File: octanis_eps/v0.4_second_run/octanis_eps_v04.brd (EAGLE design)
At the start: 61.9 x 49.5 mm, 101 parts, among them IC1 OPA2333DGK, IC5 OPA2333DGK, IC7 OPA2333DGK, IC9 OPA2333DGK, Q1 FC-12M, Q2 N-HEXFET-2D_SOT232-, Q3 N-HEXFET-2D_SOT232-, Q4 N-HEXFET-2D_SOT232-

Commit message: various corrections on EPS v0.3, new v0.4 for second run
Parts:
- removed A_EXT: (no value), jumper:JP4
- removed R37: 50m, rcl:R1206
- added BT_CHG, DSP_CMD: (no value), pinhead:1X01
- added JP2: (no value), jumper:JP4Q
- added U$9: 50m, Octanis1_EPS:4PADS_RESISTOR
- moved R3 0.74 mm to (50.1, 51.4)
- moved R25 0.64 mm to (46.4, 33.6)
- moved R12 0.31 mm to (26.1, 31.8)
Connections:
- new net N$38: R38.1, U$9.I2
- new net N$40: R39.1, U$9.I1
- net A_EXT1: now also JP2.7; no longer A_EXT.4
- net A_EXT2: now also JP2.5; no longer A_EXT.3
- net A_EXT3: now also JP2.3; no longer A_EXT.2
- net A_EXT4: now also JP2.1; no longer A_EXT.1
- net BT+: now also U$9.V1; no longer R37.1, R39.1
- net BT_CHG: now also BT_CHG.1, U$9.V2; no longer R37.2, R38.1
- net GND: now also JP2.2, JP2.4, JP2.6, JP2.8
- net N$45: now also DSP_CMD.1
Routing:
- net BT+: track 129.7 -> 121.5 mm
- net N$40: track 0.00 -> 6.17 mm
- net N$45: track 15.8 -> 17.9 mm
- net N$38: track 0.00 -> 1.85 mm
- net A_EXT4: track 12.8 -> 11.2 mm
- net A_EXT3: track 11.2 -> 9.67 mm
- net EN_HEAT1: track 31.4 -> 32.8 mm
- net BT_CHG: track 2.16 -> 3.38 mm
- net N$12: track 88.9 -> 89.9 mm
- net A_EXT1: track 10.3 -> 9.39 mm
- net A_EXT2: track 11.0 -> 10.2 mm
- net N$23: track 35.2 -> 35.9 mm
- net EN_HEAT3: track 17.4 -> 16.7 mm
- net N$37: track 29.0 -> 29.7 mm
- net SC+: track 12.0 -> 11.3 mm
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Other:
- board text added: "GND1"
- board text added: "GND2"
- board text added: "GND3"
- board text added: "GND4"
- board text added: "Octanis_EPS v0.4"
- board text removed: "Octanis_EPS v0.3"

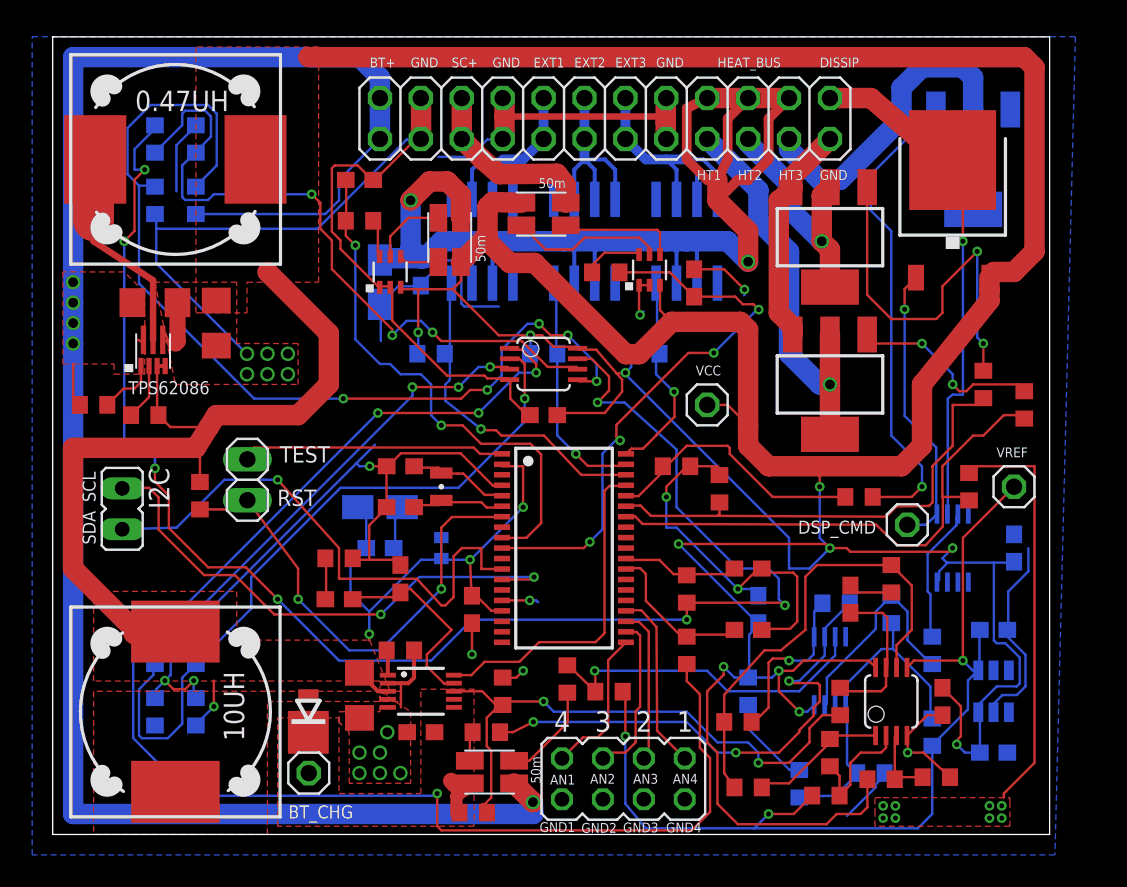
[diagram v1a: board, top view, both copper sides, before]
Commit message: thicker analog tracks for CHGCMD, better analog Grounding (same ref), regenerated gerbers. Checked with Beat
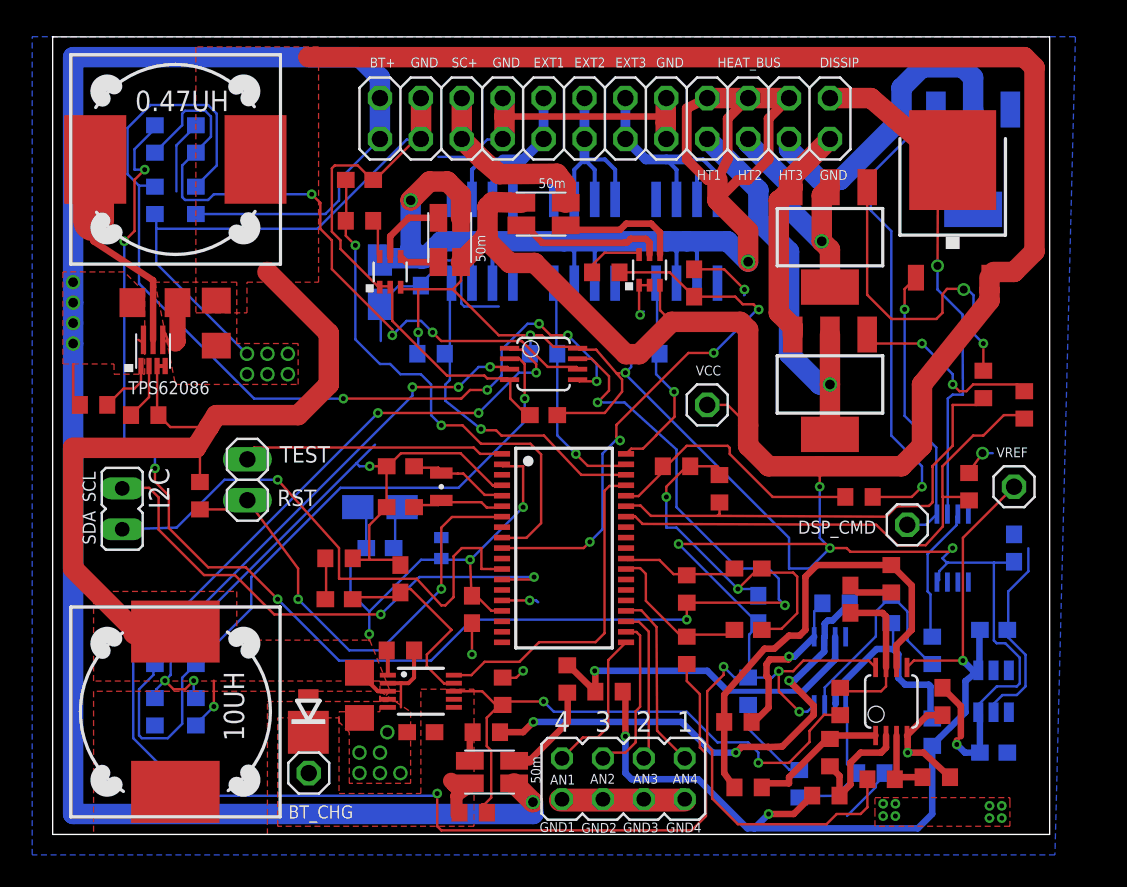
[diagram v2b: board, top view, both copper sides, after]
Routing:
- net GND: track 252.0 -> 235.9 mm, vias 29 -> 30
- net N$31: track 24.4 -> 20.5 mm
- net DISSIP: track 31.9 -> 35.3 mm
- net VREF: track 61.2 -> 60.0 mm
- net N$17: track 32.3 -> 31.2 mm
- net N$20: track 12.4 -> 13.4 mm

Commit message: modified silk screen for EPS
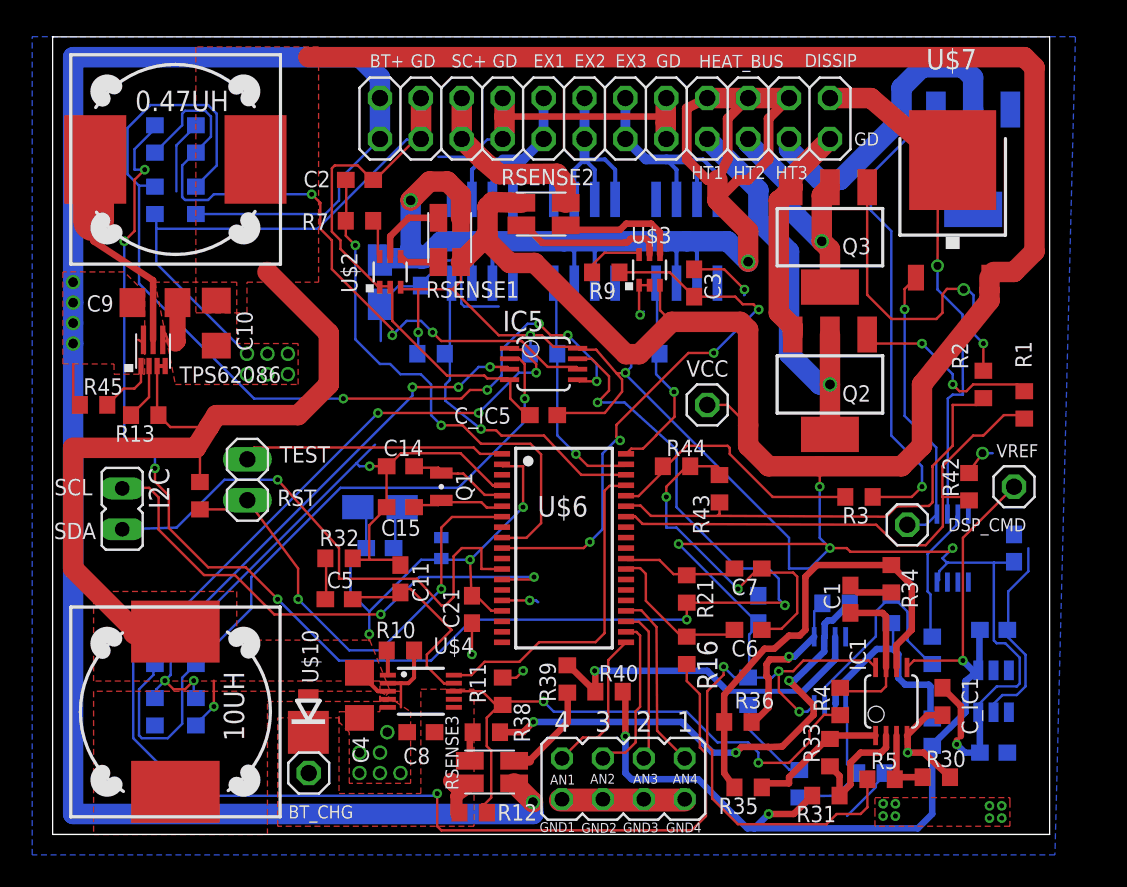
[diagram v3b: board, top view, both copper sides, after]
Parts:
- RSENSE2: value 50m -> RSENSE2
- RSENSE3: value 50m -> RSENSE3
- R_SENSE1: value 50m -> RSENSE1
- renumbered FERRITE_BEAD to FERRITE, U$1 to R_SENSE1, U$8 to RSENSE2, U$9 to RSENSE3
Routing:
- net GND: track 235.9 -> 234.6 mm
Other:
- board text added: "EX1"
- board text added: "EX2"
- board text added: "EX3"
- board text added: "GD"
- board text added: "TPS2022D"
- board text removed: "EXT1"
- board text removed: "EXT2"
- board text removed: "EXT3"
- board text removed: "GND"

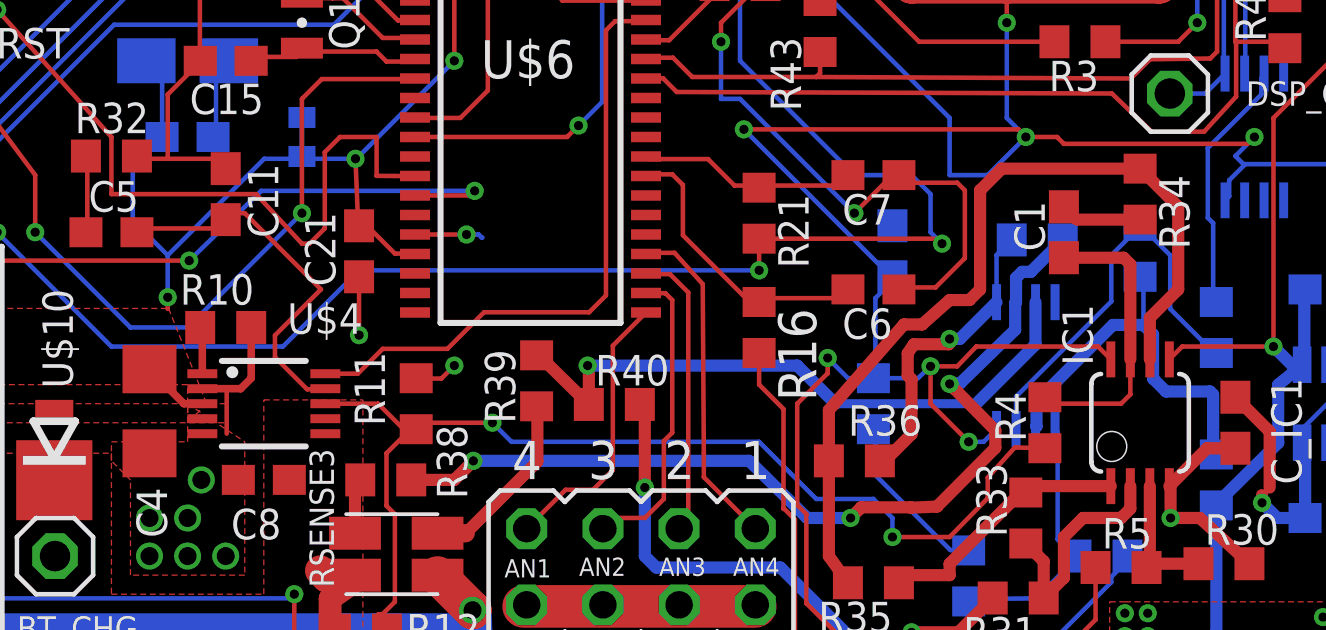
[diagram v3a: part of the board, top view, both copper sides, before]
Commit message: added pull down on boost Cvtr enable pin, C1 and R34 in parallel, Note that Rsense = 10 mOhms instead of 50mOhms at the entry of the INA213 current sensors, Rsense 3 still at 50mOhms
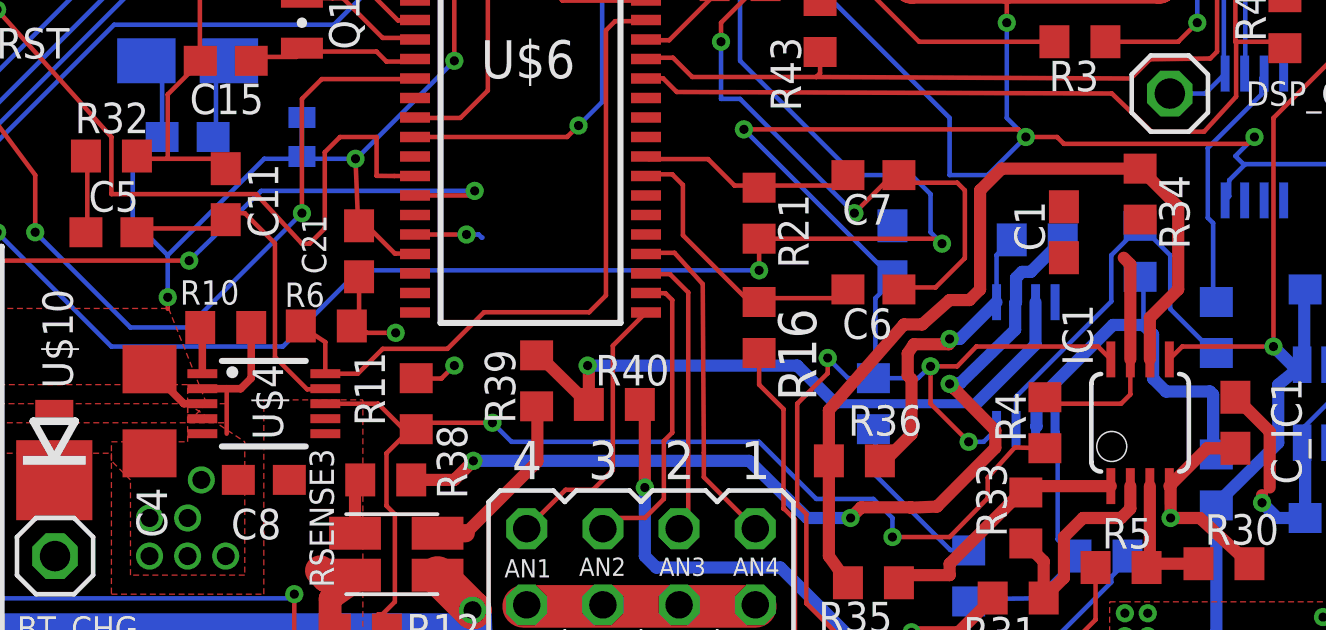
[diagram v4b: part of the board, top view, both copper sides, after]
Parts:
- added R6: 100k, rcl:R0603
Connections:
- removed net N$27: C1.2, R34.2
- net CHG_CMD: now also R34.2
- net EN_CHG: now also R6.1
- net GND: now also R6.2
- net N$11: now also C1.2
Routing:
- net N$27: track 2.72 -> 0.00 mm
- net EN_CHG: track 20.8 -> 22.8 mm
- net CHG_CMD: track 9.81 -> 7.82 mm
- net GND: track 234.6 -> 236.0 mm
- net N$8: track 12.6 -> 11.3 mm

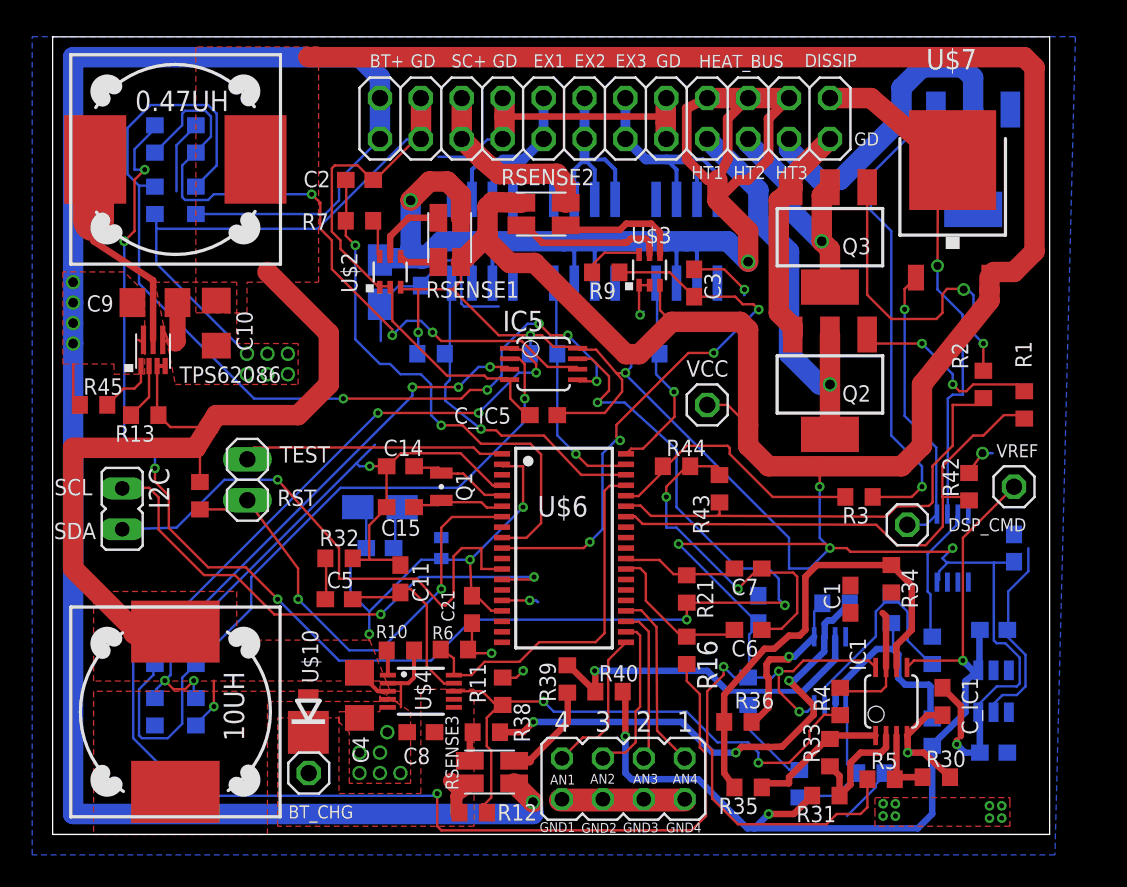
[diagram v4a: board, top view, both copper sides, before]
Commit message: changed ADR127 1.25V ref for MAX6190BESA (lower power), added 2 pins with pull down for main board sleep, DRC checked. One OPA2333 need to be changed on disispation circuit.
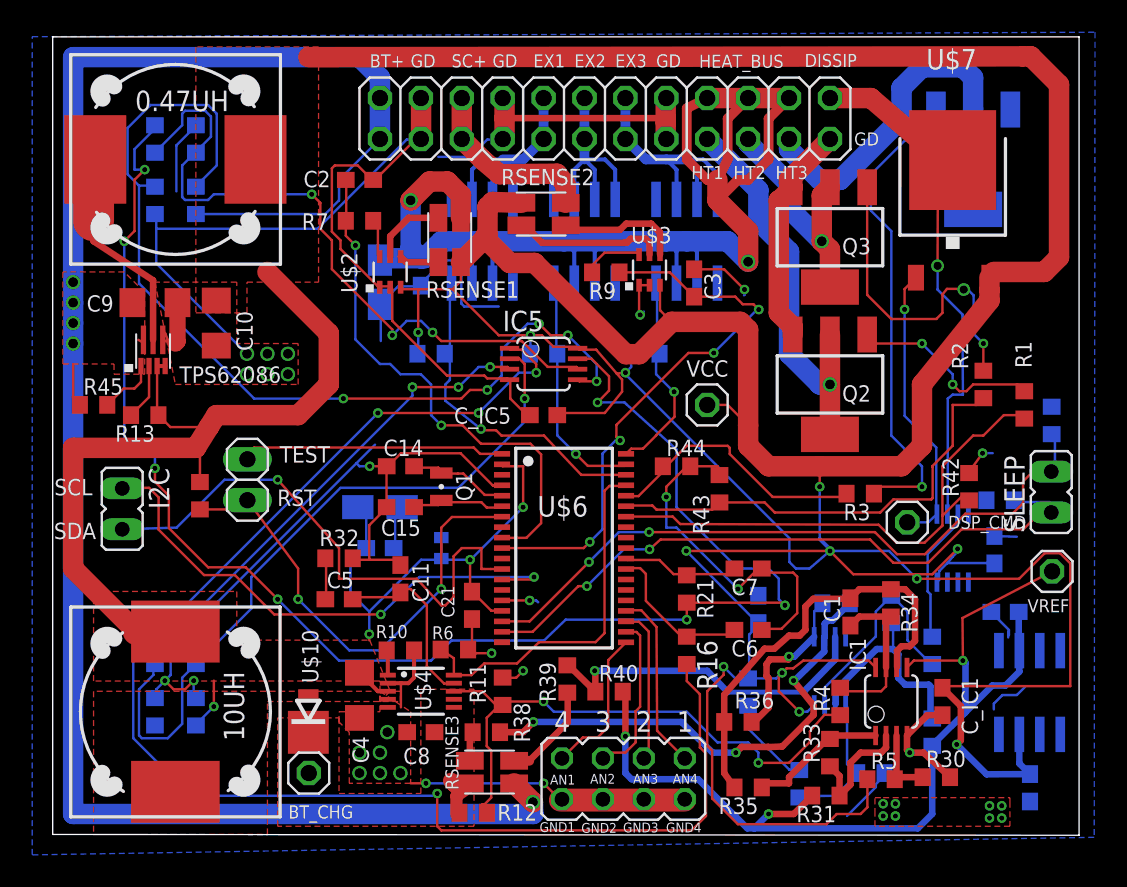
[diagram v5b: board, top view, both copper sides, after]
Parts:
- removed U$19: ADR127B, Octanis1_EPS:TSOT23-6
- added R37, R8: 100k, rcl:R0603
- added SLEEP: (no value), jumper:JP1
- added U$1: MAX6190BESA, Octanis1_EPS:SO8
- C28: value 100nF -> 2.2nF
- moved VREF 5.76 mm to (62.1, 46.8)
- moved C27 3.14 mm to (60.7, 33.4), turned to 90 degrees
- moved R34 1.50 mm to (52.0, 44.9)
- moved C28 1.32 mm to (59.1, 44.3), turned to 180 degrees
- moved C_IC9 1.22 mm to (58.5, 48.2)
- moved C1 0.79 mm to (49.5, 44.3)
- moved C21 0.25 mm to (26.0, 44.7)
- moved R3 0.22 mm to (50.1, 51.6)
- moved DSP_CMD 0.15 mm to (53.1, 49.9)
- moved R24 0.05 mm to (43.2, 39.3)
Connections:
- new net N$27: R8.1, SLEEP.1, U$6.18
- new net N$36: R37.1, SLEEP.2, U$6.17
- net GND: now also R37.2, R8.2, U$1.4; no longer U$19.2
- net VCC: now also U$1.3; no longer U$19.3
- net VREF: now also U$1.6; no longer U$19.4
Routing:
- net N$36: track 0.00 -> 42.6 mm, vias 0 -> 2
- net N$27: track 0.00 -> 41.4 mm, vias 0 -> 2
- net VCC: track 358.5 -> 385.3 mm, vias 15 -> 16
- net GND: track 236.0 -> 239.7 mm, vias 30 -> 32
- net CHG_CMD: track 7.82 -> 10.3 mm
- net N$11: track 29.0 -> 26.7 mm
- net VREF: track 60.0 -> 61.6 mm
- net EN_HEAT2: track 29.2 -> 28.4 mm
- net N$17: track 31.2 -> 30.5 mm
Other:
- board size 61.9 x 49.5 mm -> 63.7 x 49.6 mm
